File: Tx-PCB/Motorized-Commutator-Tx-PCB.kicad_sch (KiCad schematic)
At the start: 18 parts, among them J1 NRF24L01, J2 Conn_01x10_Female, J3 Conn_01x14_Female, U1 LEFT_STICK, U2 Teensy4.0, U3 LD1117S33TR_SOT223, U4 RIGHT_STICK

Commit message: Corrected Analog connections to Teensy
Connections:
- net AUTO_MODE: now also J2.1 (Pin_1), U2.8; no longer J3.4 (Pin_4), U2.16
- net LEFT_H: now also J3.4 (Pin_4), U2.16; no longer J2.5 (Pin_5), U2.4
- net LEFT_V: now also J3.5 (Pin_5), U2.17; no longer J2.6 (Pin_6), U2.3
- net MANUAL_MODE: now also J2.2 (Pin_2), U2.7; no longer J3.5 (Pin_5), U2.17
- new net: J2.5 (Pin_5), U2.4
- new net: J2.6 (Pin_6), U2.3
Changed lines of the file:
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@@
   (junction (at 109.22 58.42) (diameter 0) (color 0 0 0 0)
   )
+  (junction (at 119.38 123.19) (diameter 0) (color 0 0 0 0)
+  )
+  (junction (at 119.38 120.65) (diameter 0) (color 0 0 0 0)
+  )
   (junction (at 170.18 100.33) (diameter 0) (color 0 0 0 0)
   )
@@
   (junction (at 170.18 110.49) (diameter 0) (color 0 0 0 0)
   )
-  (junction (at 119.38 110.49) (diameter 0) (color 0 0 0 0)
-  )
   (junction (at 170.18 115.57) (diameter 0) (color 0 0 0 0)
   )
@@
   )
   (junction (at 135.89 58.42) (diameter 0) (color 0 0 0 0)
-  )
-  (junction (at 119.38 113.03) (diameter 0) (color 0 0 0 0)
   )
   (junction (at 119.38 115.57) (diameter 0) (color 0 0 0 0)
@@
     (stroke (width 0) (type default) (color 0 0 0 0))
   )
+  (wire (pts (xy 107.95 119.38) (xy 119.38 119.38))
+    (stroke (width 0) (type default) (color 0 0 0 0))
+  )
   (wire (pts (xy 170.18 133.35) (xy 171.45 133.35))
     (stroke (width 0) (type default) (color 0 0 0 0))
@@
     (stroke (width 0) (type default) (color 0 0 0 0))
   )
-  (wire (pts (xy 119.38 111.76) (xy 119.38 113.03))
-    (stroke (width 0) (type default) (color 0 0 0 0))
-  )
   (wire (pts (xy 109.22 48.26) (xy 109.22 50.8))
     (stroke (width 0) (type default) (color 0 0 0 0))
@@
     (stroke (width 0) (type default) (color 0 0 0 0))
   )
-  (wire (pts (xy 119.38 110.49) (xy 127 110.49))
+  (wire (pts (xy 118.11 110.49) (xy 127 110.49))
     (stroke (width 0) (type default) (color 0 0 0 0))
   )
@@
     (stroke (width 0) (type default) (color 0 0 0 0))
   )
+  (wire (pts (xy 119.38 123.19) (xy 127 123.19))
+    (stroke (width 0) (type default) (color 0 0 0 0))
+  )
   (wire (pts (xy 241.3 105.41) (xy 245.11 105.41))
     (stroke (width 0) (type default) (color 0 0 0 0))
@@
     (stroke (width 0) (type default) (color 0 0 0 0))
   )
+  (wire (pts (xy 107.95 121.92) (xy 119.38 121.92))
+    (stroke (width 0) (type default) (color 0 0 0 0))
+  )
   (wire (pts (xy 170.18 102.87) (xy 171.45 102.87))
     (stroke (width 0) (type default) (color 0 0 0 0))
@@
     (stroke (width 0) (type default) (color 0 0 0 0))
   )
-  (wire (pts (xy 118.11 113.03) (xy 119.38 113.03))
-    (stroke (width 0) (type default) (color 0 0 0 0))
-  )
   (wire (pts (xy 170.18 114.3) (xy 181.61 114.3))
     (stroke (width 0) (type default) (color 0 0 0 0))
@@
     (stroke (width 0) (type default) (color 0 0 0 0))
   )
+  (wire (pts (xy 119.38 119.38) (xy 119.38 120.65))
+    (stroke (width 0) (type default) (color 0 0 0 0))
+  )
+  (wire (pts (xy 119.38 120.65) (xy 127 120.65))
+    (stroke (width 0) (type default) (color 0 0 0 0))
+  )
   (wire (pts (xy 162.56 102.87) (xy 170.18 102.87))
     (stroke (width 0) (type default) (color 0 0 0 0))
   )
-  (wire (pts (xy 119.38 113.03) (xy 127 113.03))
+  (wire (pts (xy 118.11 113.03) (xy 127 113.03))
     (stroke (width 0) (type default) (color 0 0 0 0))
   )
@@
     (stroke (width 0) (type default) (color 0 0 0 0))
   )
-  (wire (pts (xy 107.95 111.76) (xy 119.38 111.76))
-    (stroke (width 0) (type default) (color 0 0 0 0))
-  )
   (wire (pts (xy 214.63 59.69) (xy 214.63 63.5))
     (stroke (width 0) (type default) (color 0 0 0 0))
@@
     (stroke (width 0) (type default) (color 0 0 0 0))
   )
-  (wire (pts (xy 118.11 120.65) (xy 127 120.65))
+  (wire (pts (xy 118.11 120.65) (xy 119.38 120.65))
     (stroke (width 0) (type default) (color 0 0 0 0))
   )
@@
     (stroke (width 0) (type default) (color 0 0 0 0))
   )
-  (wire (pts (xy 119.38 109.22) (xy 119.38 110.49))
-    (stroke (width 0) (type default) (color 0 0 0 0))
-  )
   (wire (pts (xy 144.78 52.07) (xy 144.78 50.8))
     (stroke (width 0) (type default) (color 0 0 0 0))
@@
     (stroke (width 0) (type default) (color 0 0 0 0))
   )
-  (wire (pts (xy 118.11 123.19) (xy 127 123.19))
+  (wire (pts (xy 118.11 123.19) (xy 119.38 123.19))
     (stroke (width 0) (type default) (color 0 0 0 0))
   )
@@
     (stroke (width 0) (type default) (color 0 0 0 0))
   )
-  (wire (pts (xy 118.11 110.49) (xy 119.38 110.49))
+  (wire (pts (xy 119.38 121.92) (xy 119.38 123.19))
     (stroke (width 0) (type default) (color 0 0 0 0))
   )
@@
   )
   (wire (pts (xy 170.18 113.03) (xy 162.56 113.03))
-    (stroke (width 0) (type default) (color 0 0 0 0))
-  )
-  (wire (pts (xy 107.95 109.22) (xy 119.38 109.22))
     (stroke (width 0) (type default) (color 0 0 0 0))
   )
@@
     )
   )
-  (global_label "LEFT_V" (shape input) (at 107.95 109.22 180) (fields_autoplaced)
-    (effects (font (size 1 1)) (justify right))
-    (property "Intersheet References" "${INTERSHEET_REFS}" (id 0) (at 101.0976 109.1575 0)
-      (effects (font (size 1 1)) (justify right) hide)
-    )
-  )
   (global_label "AUTO_MODE" (shape input) (at 78.74 57.15 0) (fields_autoplaced)
     (effects (font (size 1 1)) (justify left))
@@
     )
   )
-  (global_label "AUTO_MODE" (shape input) (at 181.61 124.46 0) (fields_autoplaced)
-    (effects (font (size 1 1)) (justify left))
-    (property "Intersheet References" "${INTERSHEET_REFS}" (id 0) (at 192.0814 124.3975 0)
-      (effects (font (size 1 1)) (justify left) hide)
-    )
-  )
   (global_label "GND" (shape input) (at 181.61 101.6 0) (fields_autoplaced)
     (effects (font (size 1 1)) (justify left))
@@
     )
   )
+  (global_label "LEFT_H" (shape input) (at 181.61 124.46 0) (fields_autoplaced)
+    (effects (font (size 1 1)) (justify left))
+    (property "Intersheet References" "${INTERSHEET_REFS}" (id 0) (at 188.6529 124.5225 0)
+      (effects (font (size 1 1)) (justify left) hide)
+    )
+  )
   (global_label "LEFT_B" (shape input) (at 107.95 114.3 180) (fields_autoplaced)
     (effects (font (size 1 1)) (justify right))
@@
     )
   )
-  (global_label "LEFT_H" (shape input) (at 107.95 111.76 180) (fields_autoplaced)
-    (effects (font (size 1 1)) (justify right))
-    (property "Intersheet References" "${INTERSHEET_REFS}" (id 0) (at 100.9071 111.6975 0)
-      (effects (font (size 1 1)) (justify right) hide)
-    )
-  )
   (global_label "3.3V" (shape input) (at 135.89 48.26 90) (fields_autoplaced)
     (effects (font (size 1 1)) (justify left))
@@
     )
   )
-  (global_label "MANUAL_MODE" (shape input) (at 181.61 121.92 0) (fields_autoplaced)
-    (effects (font (size 1 1)) (justify left))
-    (property "Intersheet References" "${INTERSHEET_REFS}" (id 0) (at 194.129 121.8575 0)
-      (effects (font (size 1 1)) (justify left) hide)
+  (global_label "MANUAL_MODE" (shape input) (at 107.95 119.38 180) (fields_autoplaced)
+    (effects (font (size 1 1)) (justify right))
+    (property "Intersheet References" "${INTERSHEET_REFS}" (id 0) (at 95.431 119.4425 0)
+      (effects (font (size 1 1)) (justify right) hide)
+    )
+  )
+  (global_label "AUTO_MODE" (shape input) (at 107.95 121.92 180) (fields_autoplaced)
+    (effects (font (size 1 1)) (justify right))
+    (property "Intersheet References" "${INTERSHEET_REFS}" (id 0) (at 97.4786 121.9825 0)
+      (effects (font (size 1 1)) (justify right) hide)
     )
   )
@@
     )
   )
+  (global_label "LEFT_V" (shape input) (at 181.61 121.92 0) (fields_autoplaced)
+    (effects (font (size 1 1)) (justify left))
+    (property "Intersheet References" "${INTERSHEET_REFS}" (id 0) (at 188.4624 121.9825 0)
+      (effects (font (size 1 1)) (justify left) hide)
+    )
+  )

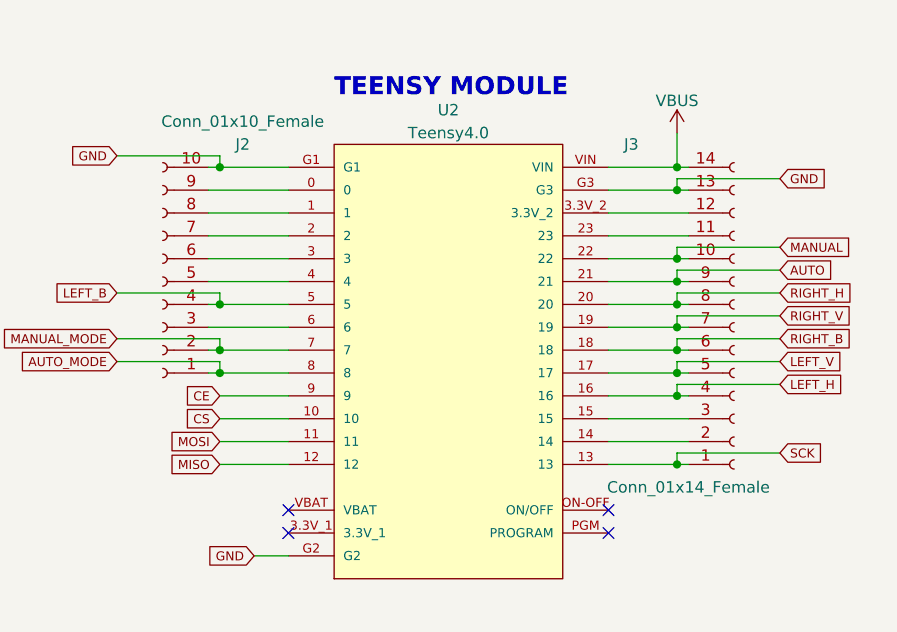
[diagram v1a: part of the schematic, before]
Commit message: Updated PCB BOMs and iBOMs
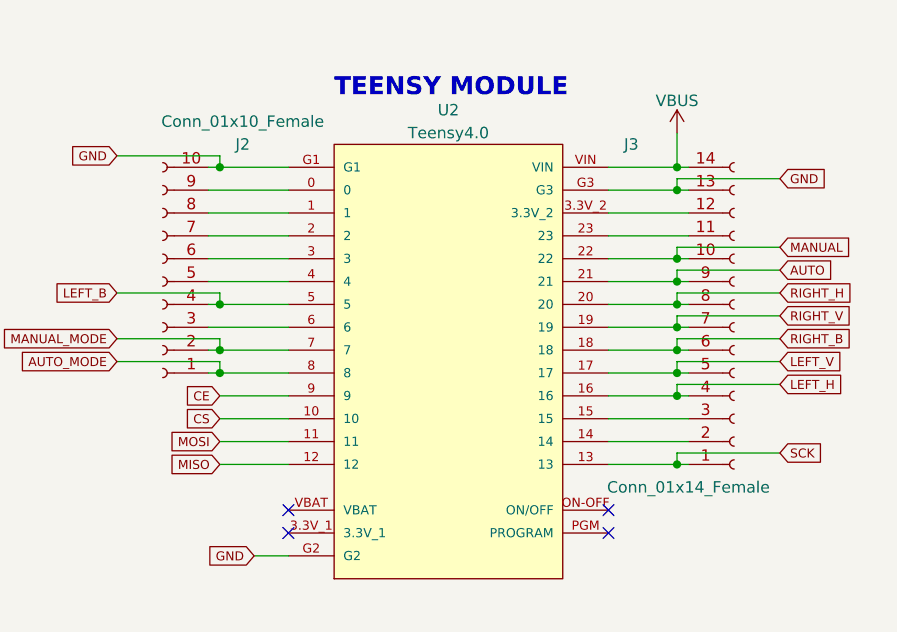
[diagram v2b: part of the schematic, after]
